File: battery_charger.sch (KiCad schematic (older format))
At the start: 27 parts

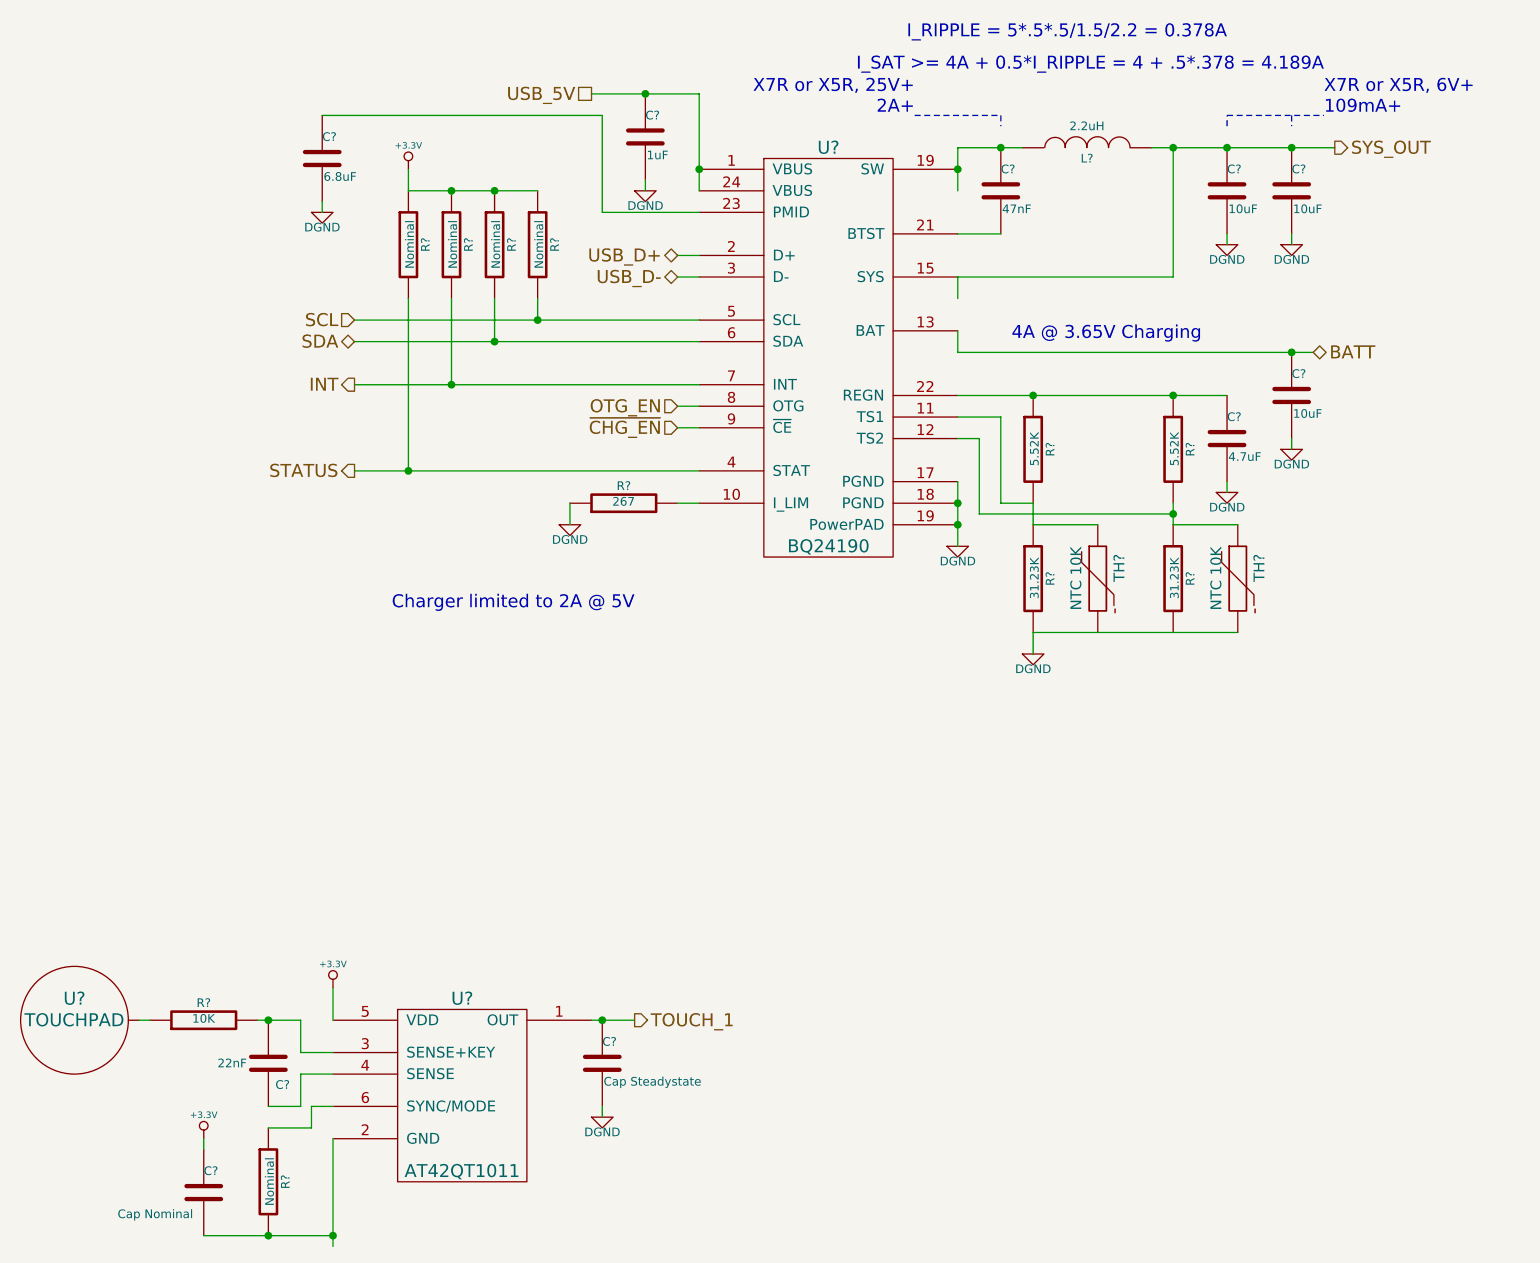
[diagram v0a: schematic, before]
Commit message: finished schematic charger, need to part out caps and inductor
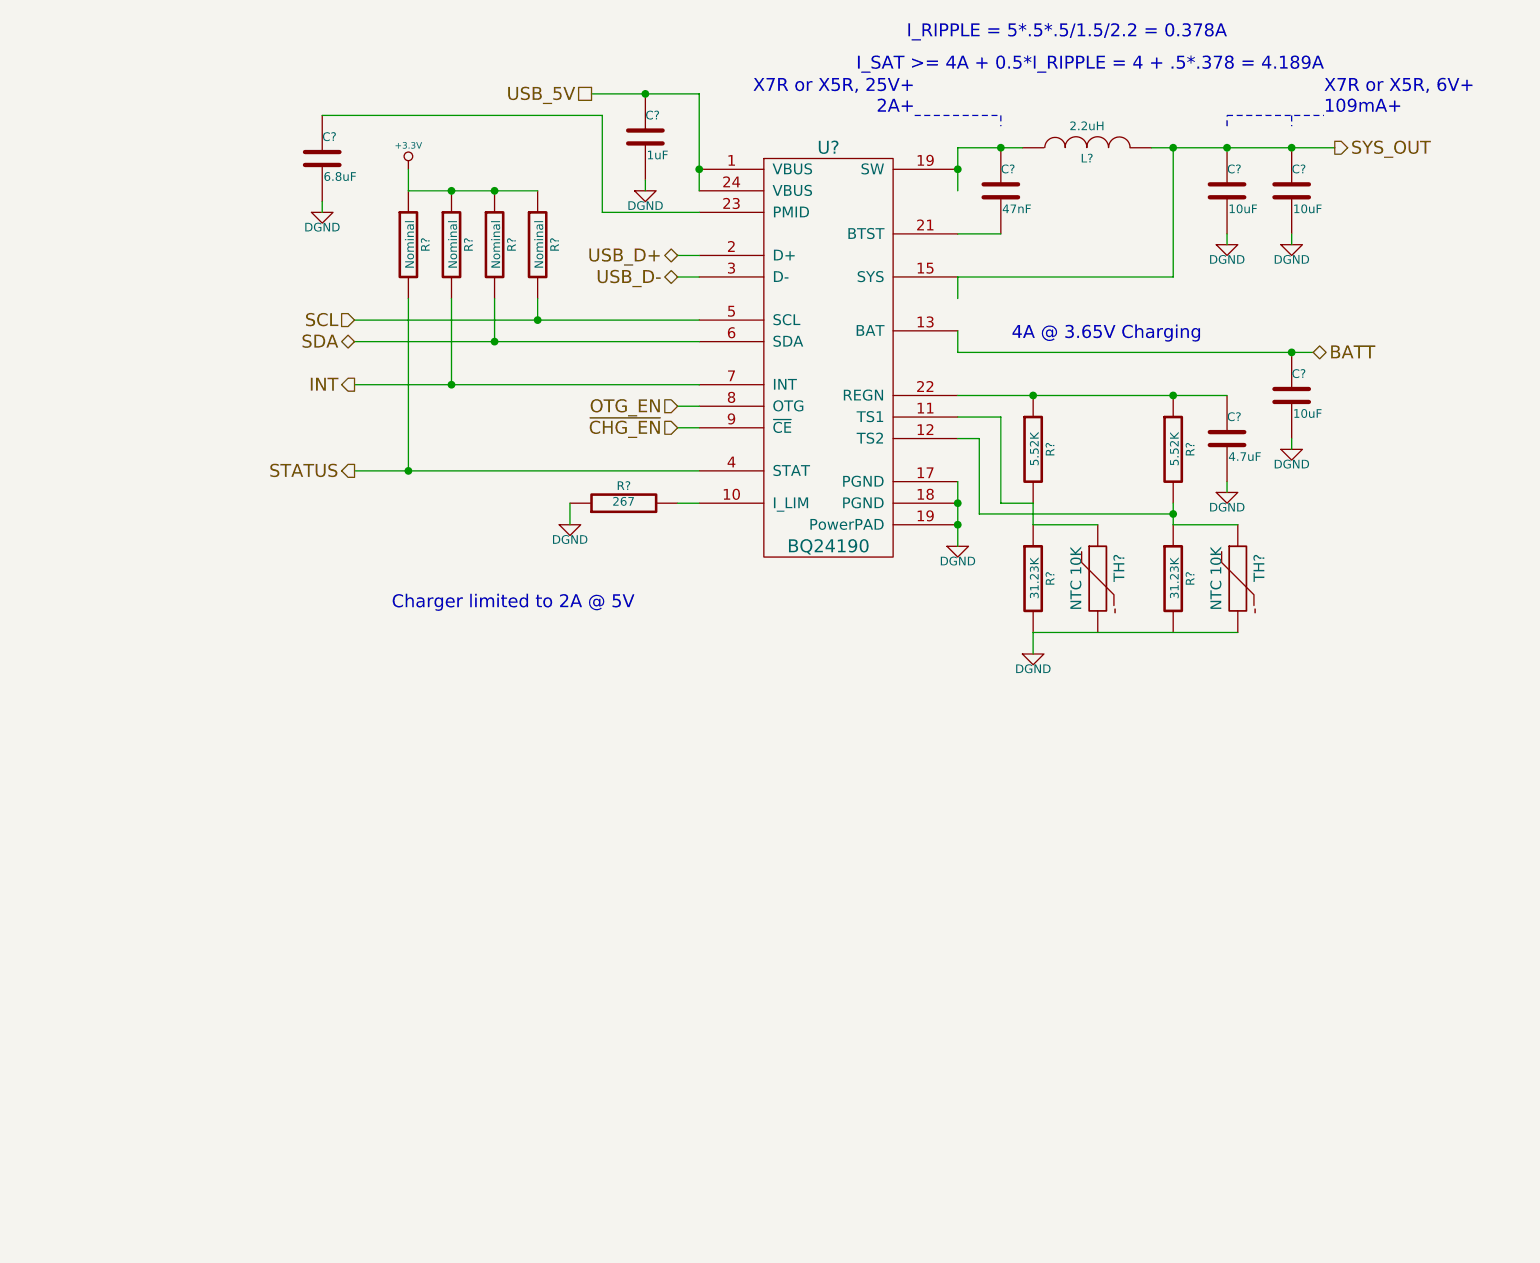
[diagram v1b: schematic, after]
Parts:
- removed C?: 22nF, ~, symbol C
- removed C?: Cap Nominal, ~, symbol C
- removed C?: Cap Steadystate, ~, symbol C
- removed R?: 10K, ~, symbol R
- removed R?: Nominal, ~, symbol R
- removed U?: AT42QT1011, symbol AT42QT1011
- removed U?: TOUCHPAD, symbol TOUCHPAD
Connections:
- net labels removed: TOUCH_1
- wire segments 66 -> 69
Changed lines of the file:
@@
 Sheet 14 18
 Title ""
-Date "13 dec 2013"
+Date "14 dec 2013"
 Rev ""
 Comp ""
@@
 USB_D-
 $Comp
-L AT42QT1011 U?
-U 1 1 5292B822
-P 3100 5600
-F 0 "U?" H 3100 5600 60  0000 C CNN
-F 1 "AT42QT1011" H 3100 4800 60  0000 C CNN
-F 2 "" H 3100 5600 60  0000 C CNN
-F 3 "" H 3100 5600 60  0000 C CNN
-	1    3100 5600
-	1    0    0    -1
-$EndComp
-$Comp
-L +3.3V #PWR?
-U 1 1 5292B828
-P 2500 5550
-F 0 "#PWR?" H 2500 5510 30  0001 C CNN
-F 1 "+3.3V" H 2500 5660 30  0000 C CNN
-F 2 "" H 2500 5550 60  0000 C CNN
-F 3 "" H 2500 5550 60  0000 C CNN
-	1    2500 5550
-	1    0    0    -1
-$EndComp
-$Comp
 L DGND #PWR?
 U 1 1 5292B82E
@@
 F 3 "" H 3600 3400 60  0000 C CNN
 	1    3600 3400
-	1    0    0    -1
-$EndComp
-$Comp
-L R R?
-U 1 1 5292B834
-P 1900 5700
-F 0 "R?" V 1980 5700 40  0000 C CNN
-F 1 "10K" V 1907 5701 40  0000 C CNN
-F 2 "~" V 1830 5700 30  0000 C CNN
-F 3 "~" H 1900 5700 30  0000 C CNN
-	1    1900 5700
-	0    -1   -1   0
-$EndComp
-$Comp
-L C C?
-U 1 1 5292B83A
-P 2200 5900
-F 0 "C?" H 2100 6000 40  0000 L CNN
-F 1 "22nF" H 2300 5900 40  0000 L CNN
-F 2 "~" H 2238 5750 30  0000 C CNN
-F 3 "~" H 2200 5900 60  0000 C CNN
-	1    2200 5900
-	-1   0    0    1
-$EndComp
-$Comp
-L TOUCHPAD U?
-U 1 1 5292B840
-P 1300 5700
-F 0 "U?" H 1300 5800 60  0000 C CNN
-F 1 "TOUCHPAD" H 1300 5700 60  0000 C CNN
-F 2 "" H 1300 5700 60  0000 C CNN
-F 3 "" H 1300 5700 60  0000 C CNN
-	1    1300 5700
-	1    0    0    -1
-$EndComp
-$Comp
-L C C?
-U 1 1 5292B858
-P 1900 6500
-F 0 "C?" H 1900 6600 40  0000 L CNN
-F 1 "Cap Nominal" H 1500 6400 40  0000 L CNN
-F 2 "~" H 1938 6350 30  0000 C CNN
-F 3 "~" H 1900 6500 60  0000 C CNN
-	1    1900 6500
-	1    0    0    -1
-$EndComp
-$Comp
-L +3.3V #PWR?
-U 1 1 5292B85E
-P 1900 6250
-F 0 "#PWR?" H 1900 6210 30  0001 C CNN
-F 1 "+3.3V" H 1900 6360 30  0000 C CNN
-F 2 "" H 1900 6250 60  0000 C CNN
-F 3 "" H 1900 6250 60  0000 C CNN
-	1    1900 6250
-	1    0    0    -1
-$EndComp
-$Comp
-L C C?
-U 1 1 5292B866
-P 3750 5900
-F 0 "C?" H 3750 6000 40  0000 L CNN
-F 1 "Cap Steadystate" H 3756 5815 40  0000 L CNN
-F 2 "~" H 3788 5750 30  0000 C CNN
-F 3 "~" H 3750 5900 60  0000 C CNN
-	1    3750 5900
-	1    0    0    -1
-$EndComp
-$Comp
-L DGND #PWR?
-U 1 1 5292B86E
-P 3750 6150
-F 0 "#PWR?" H 3750 6150 40  0001 C CNN
-F 1 "DGND" H 3750 6080 40  0000 C CNN
-F 2 "" H 3750 6150 60  0000 C CNN
-F 3 "" H 3750 6150 60  0000 C CNN
-	1    3750 6150
-	1    0    0    -1
-$EndComp
-Text HLabel 3900 5700 2    60   Output ~ 0
-TOUCH_1
-$Comp
-L R R?
-U 1 1 5292B877
-P 2200 6450
-F 0 "R?" V 2280 6450 40  0000 C CNN
-F 1 "Nominal" V 2207 6451 40  0000 C CNN
-F 2 "~" V 2130 6450 30  0000 C CNN
-F 3 "~" H 2200 6450 30  0000 C CNN
-	1    2200 6450
 	1    0    0    -1
 $EndComp
@@
 $EndComp
 Wire Wire Line
-	1650 5700 1600 5700
-Wire Wire Line
-	2150 5700 2350 5700
-Wire Wire Line
-	2350 5700 2350 5850
-Wire Wire Line
-	2350 5850 2500 5850
-Wire Wire Line
-	2200 6100 2350 6100
-Wire Wire Line
-	2350 6100 2350 5950
-Wire Wire Line
-	2350 5950 2500 5950
-Connection ~ 2200 5700
-Wire Wire Line
-	2500 5550 2500 5700
-Wire Wire Line
-	2500 6250 2500 6750
-Wire Wire Line
-	2400 6200 2400 6100
-Wire Wire Line
-	2400 6100 2500 6100
-Connection ~ 2500 6700
-Wire Wire Line
-	2400 6200 2200 6200
-Wire Wire Line
-	1900 6700 2500 6700
-Wire Wire Line
-	1900 6250 1900 6300
-Connection ~ 2200 6700
-Wire Wire Line
-	3700 5700 3900 5700
-Wire Wire Line
-	3750 6100 3750 6150
-Connection ~ 3750 5700
-Wire Wire Line
-	5400 3200 5400 3500
+	5400 3200 5400 3300
+Wire Wire Line
+	5400 3300 5400 3400
+Wire Wire Line
+	5400 3400 5400 3500
 Connection ~ 5400 3300
 Connection ~ 5400 3400
@@
 	3600 3300 3600 3400
 Wire Wire Line
-	5400 2800 6650 2800
+	5400 2800 5750 2800
+Wire Wire Line
+	5750 2800 6400 2800
+Wire Wire Line
+	6400 2800 6650 2800
 Connection ~ 5750 2800
 Wire Wire Line
@@
 	5600 3300 5750 3300
 Wire Wire Line
-	6400 3300 6400 3400
+	6400 3300 6400 3350
+Wire Wire Line
+	6400 3350 6400 3400
 Connection ~ 6400 3350
 Wire Wire Line
@@
 	3450 2350 3450 2450
 Wire Wire Line
-	2600 2450 4200 2450
-Wire Wire Line
-	2600 2550 4200 2550
+	2600 2450 3450 2450
+Wire Wire Line
+	3450 2450 4200 2450
+Wire Wire Line
+	2600 2550 3250 2550
+Wire Wire Line
+	3250 2550 4200 2550
 Wire Wire Line
 	3250 2550 3250 2350
@@
 	3050 2350 3050 2750
 Wire Wire Line
-	2600 2750 4200 2750
+	2600 2750 3050 2750
+Wire Wire Line
+	3050 2750 4200 2750
 Text HLabel 2600 2450 0    60   Input ~ 0
 SCL
@@
 	4100 2250 4200 2250
 Wire Wire Line
-	4200 1400 4200 1850
+	4200 1400 4200 1750
+Wire Wire Line
+	4200 1750 4200 1850
 $Comp
 L C C?
@@
 Connection ~ 4200 1750
 Wire Wire Line
-	3700 1400 4200 1400
+	3700 1400 3950 1400
+Wire Wire Line
+	3950 1400 4200 1400
 Connection ~ 3950 1400
 $Comp
@@
 $EndComp
 Wire Wire Line
-	2850 1850 3450 1850
+	2850 1850 3050 1850
+Wire Wire Line
+	3050 1850 3250 1850
+Wire Wire Line
+	3250 1850 3450 1850
 Connection ~ 3250 1850
 $Comp
@@
 Connection ~ 3050 1850
 Wire Wire Line
-	2600 3150 4200 3150
+	2600 3150 2850 3150
+Wire Wire Line
+	2850 3150 4200 3150
 Wire Wire Line
 	2850 2350 2850 3150
@@
 	5400 2500 5400 2600
 Wire Wire Line
-	5400 2600 7050 2600
+	5400 2600 6950 2600
+Wire Wire Line
+	6950 2600 7050 2600
 Text HLabel 7050 2600 2    60   BiDi ~ 0
 BATT
@@
 	5400 2050 5600 2050
 Wire Wire Line
-	5400 1650 5400 1850
-Wire Wire Line
-	5400 1650 5700 1650
+	5400 1650 5400 1750
+Wire Wire Line
+	5400 1750 5400 1850
+Wire Wire Line
+	5400 1650 5600 1650
+Wire Wire Line
+	5600 1650 5700 1650
 Connection ~ 5400 1750
 Connection ~ 5600 1650
@@
 	5400 2350 5400 2250
 Wire Wire Line
-	6300 1650 7150 1650
+	6300 1650 6400 1650
+Wire Wire Line
+	6400 1650 6650 1650
+Wire Wire Line
+	6650 1650 6950 1650
+Wire Wire Line
+	6950 1650 7150 1650
 Wire Wire Line
 	6400 1650 6400 2250
